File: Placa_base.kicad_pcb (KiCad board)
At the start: 2 copper layers, 200 x 100 mm, 214 parts, among them J1 SWD/STLINK, J10 Interfaz con entradas digital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, J11 I2C1, J12 I2C3, J13 CAN1, J14 SPI1, J15 Conn_02x08_Odd_Even, J2 Bateria, J3 Entrada 24V, J4 RS-485, J5 TV_6V, J6 AN1, J7 AN2, J8 Micro_SD_Card_Det_Hirose_DM3AT, J9 Salidas 5V, Q1 MMBT3904, Q2 MMBT3904, Q3 MMBT3904, Q4 AO3401, Q5 AO3401, SW1 SW_Push, SW2 SW_Push, SW3 SW_Push, U1 STM32F407VGTx, U10 MCP6L04T-E/ST, U11 74HCT541, U2 DC-DC_Step-Down, U3 AZ1117-3.3, U4 AZ1117-3.3, U5 RFM-0505S, U6 ISO1412, U7 NodeMCU_1.0_(ESP-12E), U8 SIM800L_modulo, U9 Modulo_A6_Mini, Y1 32.768KHz, Y2 8MHz

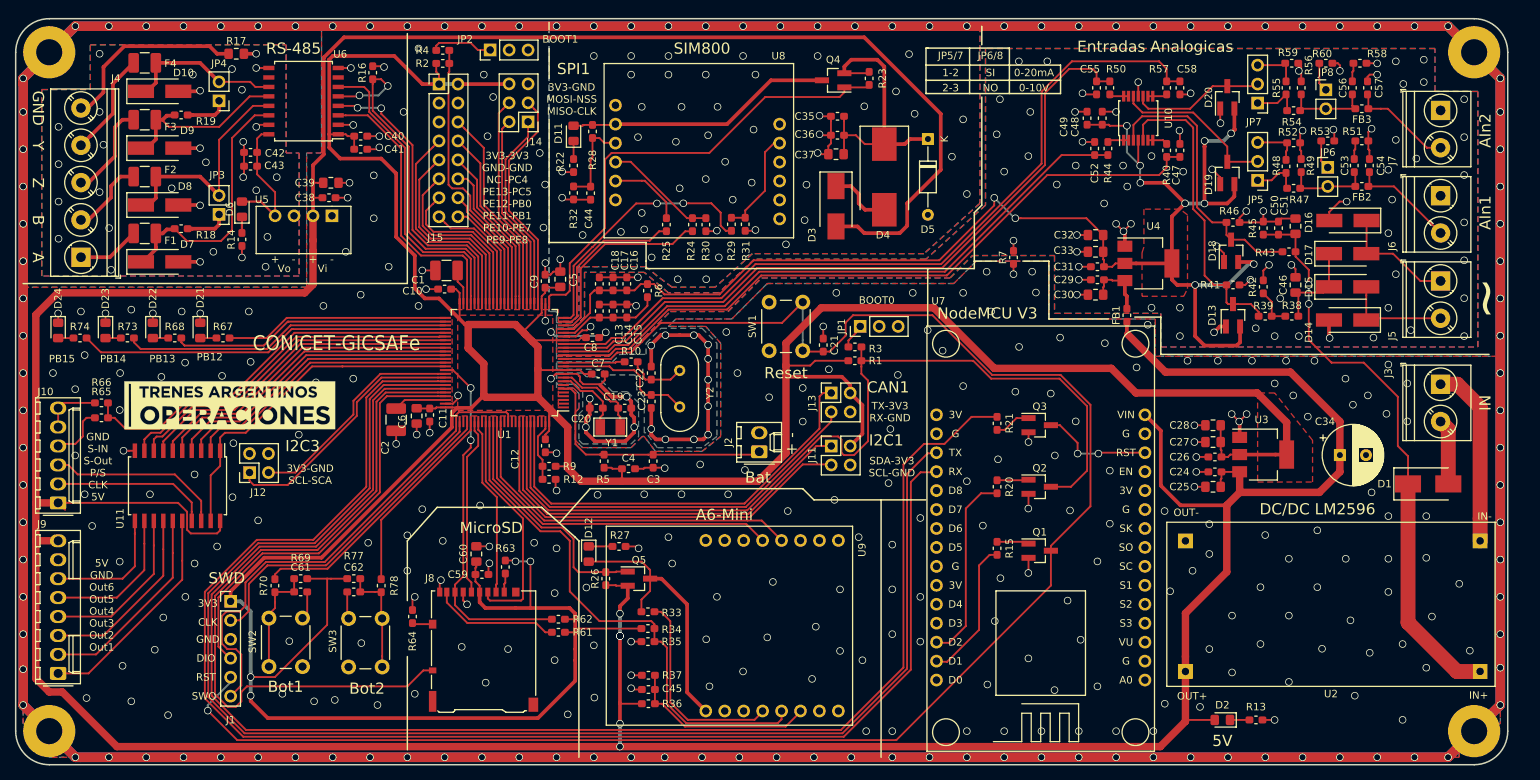
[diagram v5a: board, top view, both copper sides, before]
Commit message: PCB 1.3. Re-ruteo de 5v, VCC, desacople, etc.
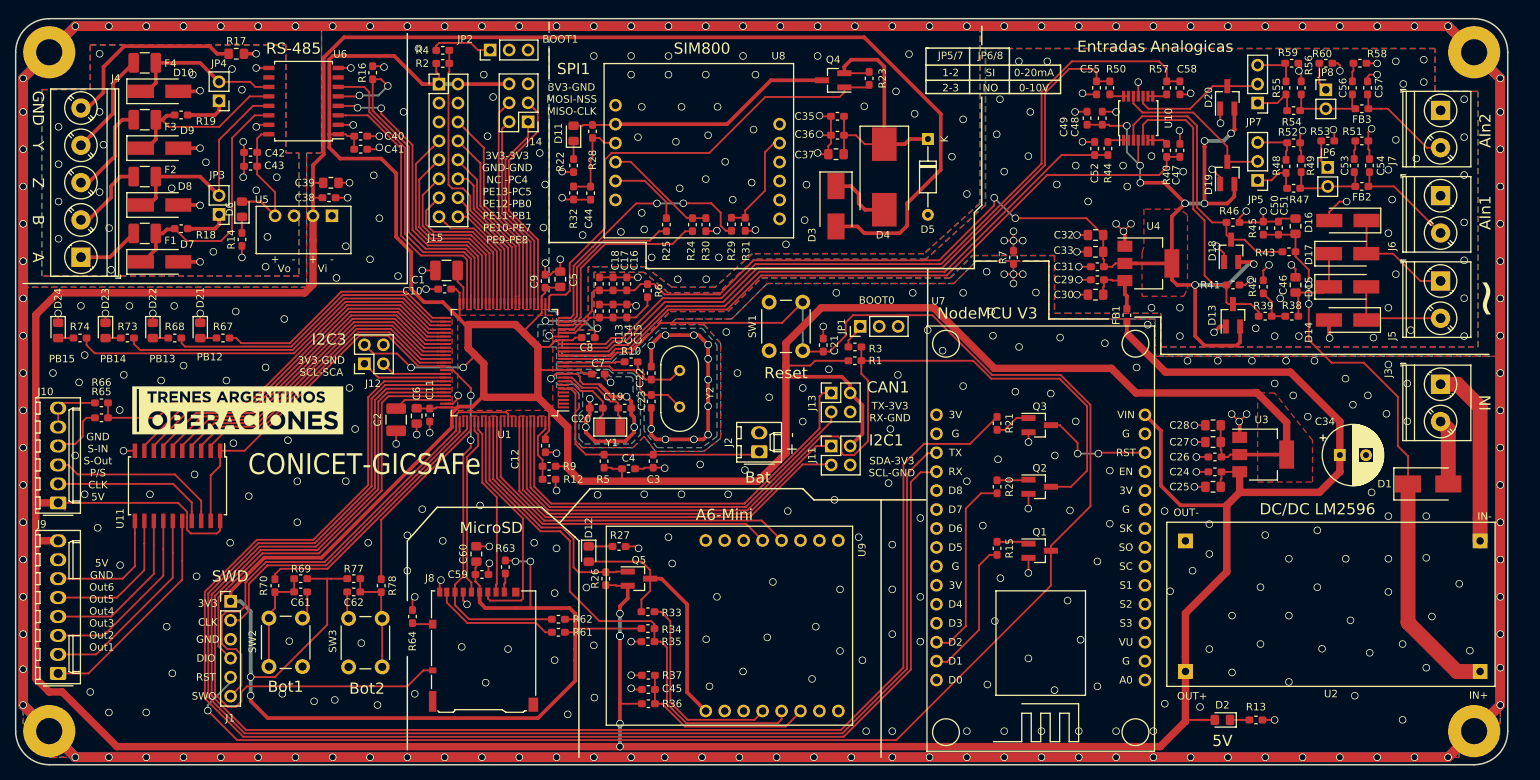
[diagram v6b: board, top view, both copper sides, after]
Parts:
- J8: footprint Connector_Card:microSD_HC_Hirose_DM3AT-SF-PEJM5 -> Propios:microSD_HC_Hirose_DM3AT-SF-PEJM5
- moved J12 21.2 mm to (116.8, 86.2)
- moved G1 1.27 mm to (99.8, 92.5)
- moved C8 0.57 mm to (146.8, 82.8)
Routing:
- net /PA8: track 34.6 -> 11.6 mm
- net /PC9: track 30.3 -> 8.88 mm
- net VDD: track 524.2 -> 540.6 mm, vias 4 -> 6
- net /LED4: track 50.2 -> 53.9 mm
- net GND: track 1344.0 -> 1347.6 mm, vias 425 -> 428
- net /LED1: track 30.1 -> 33.5 mm
- net /LED3: track 44.0 -> 47.2 mm
- net /LED2: track 37.5 -> 40.6 mm
- net /PD12: track 43.0 -> 45.9 mm
- net /PD15: track 38.7 -> 41.6 mm
- net /PD14: track 40.2 -> 43.0 mm
- net /PC6: track 37.4 -> 40.1 mm
- net /PD13: track 41.8 -> 44.4 mm
- net /PD9: track 47.6 -> 50.2 mm
- net /PD10: track 46.4 -> 48.8 mm
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
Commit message: Se corrige ruteo de pads en U11
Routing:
- net /PC7: track 48.2 -> 49.1 mm
- net /PC6: track 40.1 -> 40.6 mm
- net /PD15: track 41.6 -> 42.1 mm

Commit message: Cambio de I2C3 por USART6
Cambio mínimo para que quede disponible la UART6
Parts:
- J12: value I2C3 -> USART6
- moved J12 2.55 mm to (119.3, 86.2), turned to 180 degrees
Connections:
- J12 pad 1: /PA8 -> /PC7
- J12 pad 3: /PC9 -> /PC6
- J15 pad 5: (no net) -> Net-(J15-Pad5)
- J8 pad 12: (no net) -> Net-(J8-Pad12)
- J8 pad 13: (no net) -> Net-(J8-Pad13)
- J8 pad 14: (no net) -> Net-(J8-Pad14)
- JP1 pad 3: (no net) -> Net-(JP1-Pad3)
- JP2 pad 3: (no net) -> Net-(JP2-Pad3)
- U1 pad 1: (no net) -> /MCU/PE2
- U1 pad 2: (no net) -> /MCU/PE3
- U1 pad 3: (no net) -> /MCU/PE4
- U1 pad 4: (no net) -> /MCU/PE5
- U1 pad 5: (no net) -> /MCU/PE6
- U1 pad 7: (no net) -> /MCU/PC13
- U1 pad 77: (no net) -> /MCU/TDI
- U1 pad 82: (no net) -> /MCU/PD1
- U1 pad 88: (no net) -> /MCU/PD7
- U1 pad 90: (no net) -> /MCU/nTRST
- U1 pad 91: (no net) -> /MCU/PB5
- U1 pad 97: (no net) -> /MCU/PE0
- U1 pad 98: (no net) -> /MCU/PE1
- U11 pad 1: /PC7 -> /PA8
- U11 pad 19: /PC7 -> /PA8
- U11 pad 2: /PC6 -> /PC9
- U6 pad 10: (no net) -> Net-(U6-Pad10)
- U6 pad 7: (no net) -> Net-(U6-Pad7)
- U7 pad 1: (no net) -> Net-(U7-Pad1)
- U7 pad 11: (no net) -> Net-(U7-Pad11)
- U7 pad 12: (no net) -> Net-(U7-Pad12)
- U7 pad 16: (no net) -> Net-(U7-Pad16)
- U7 pad 2: (no net) -> Net-(U7-Pad2)
- U7 pad 20: (no net) -> Net-(U7-Pad20)
- U7 pad 21: (no net) -> Net-(U7-Pad21)
- U7 pad 22: (no net) -> Net-(U7-Pad22)
- U7 pad 23: (no net) -> Net-(U7-Pad23)
- U7 pad 25: (no net) -> Net-(U7-Pad25)
- U7 pad 26: (no net) -> Net-(U7-Pad26)
- U7 pad 27: (no net) -> Net-(U7-Pad27)
- U7 pad 3: (no net) -> Net-(U7-Pad3)
- U7 pad 30: (no net) -> Net-(U7-Pad30)
- U7 pad 4: (no net) -> Net-(U7-Pad4)
- U7 pad 5: (no net) -> Net-(U7-Pad5)
- U7 pad 6: (no net) -> Net-(U7-Pad6)
- U7 pad 7: (no net) -> Net-(U7-Pad7)
- U7 pad 8: (no net) -> Net-(U7-Pad8)
- U7 pad 9: (no net) -> Net-(U7-Pad9)
- U8 pad 1: (no net) -> Net-(U8-Pad1)
- U8 pad 10: (no net) -> Net-(U8-Pad10)
- U8 pad 12: (no net) -> Net-(U8-Pad12)
- U8 pad 7: (no net) -> Net-(U8-Pad7)
- U8 pad 8: (no net) -> Net-(U8-Pad8)
- U8 pad 9: (no net) -> Net-(U8-Pad9)
- U9 pad 10: (no net) -> Net-(U9-Pad10)
- U9 pad 11: (no net) -> Net-(U9-Pad11)
- U9 pad 15: (no net) -> Net-(U9-Pad15)
- U9 pad 16: (no net) -> Net-(U9-Pad16)
- U9 pad 2: (no net) -> Net-(U9-Pad2)
- U9 pad 3: (no net) -> Net-(U9-Pad3)
- U9 pad 7: (no net) -> Net-(U9-Pad7)
- U9 pad 8: (no net) -> Net-(U9-Pad8)
- U9 pad 9: (no net) -> Net-(U9-Pad9)
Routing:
- net /PC7: track 49.1 -> 8.89 mm
- net /PA8: track 11.6 -> 45.1 mm
- net /PC6: track 40.6 -> 9.32 mm
- net /PC9: track 8.88 -> 36.7 mm
- net /PD11: track 47.8 -> 47.2 mm
- net /PD12: track 46.3 -> 45.7 mm
- net /PD13: track 44.9 -> 44.3 mm
- net /PD14: track 43.5 -> 42.9 mm
- net /PD15: track 42.1 -> 41.5 mm
- net /LED1: track 33.5 -> 33.0 mm
- net /LED2: track 40.6 -> 40.0 mm
- net /LED3: track 47.2 -> 46.7 mm
- net /LED4: track 53.9 -> 53.3 mm
- net /PD8: track 55.0 -> 54.5 mm
- net /PD9: track 50.6 -> 50.1 mm
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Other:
- board text added: "GND-TX 3V3-RX"
- board text added: "USART6"
- board text removed: "3V3-GND SCL-SCA"
- board text removed: "I2C3"
